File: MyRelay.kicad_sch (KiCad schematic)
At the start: 8 parts, among them K3 Relay, Q1 2N7002, Q2 2N7002

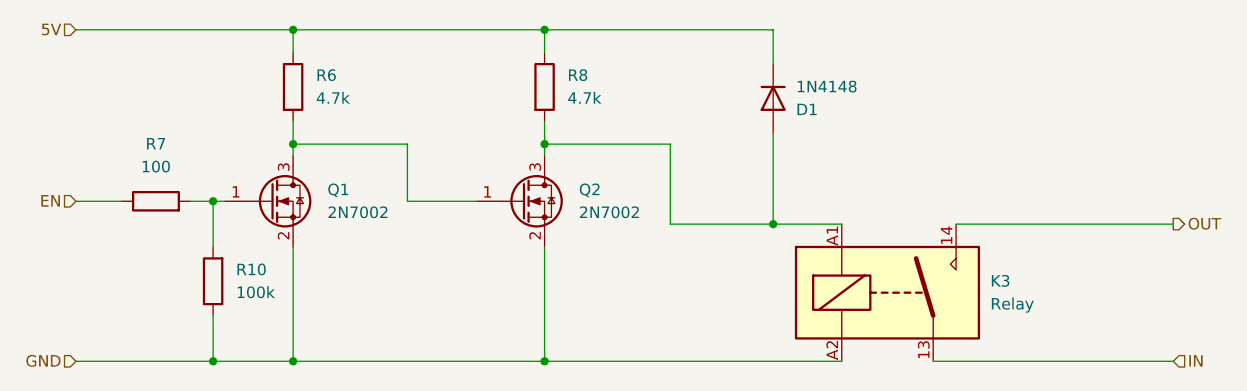
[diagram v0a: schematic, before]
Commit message: update footprints, add 230v module, use SSRs and do some basic layouting
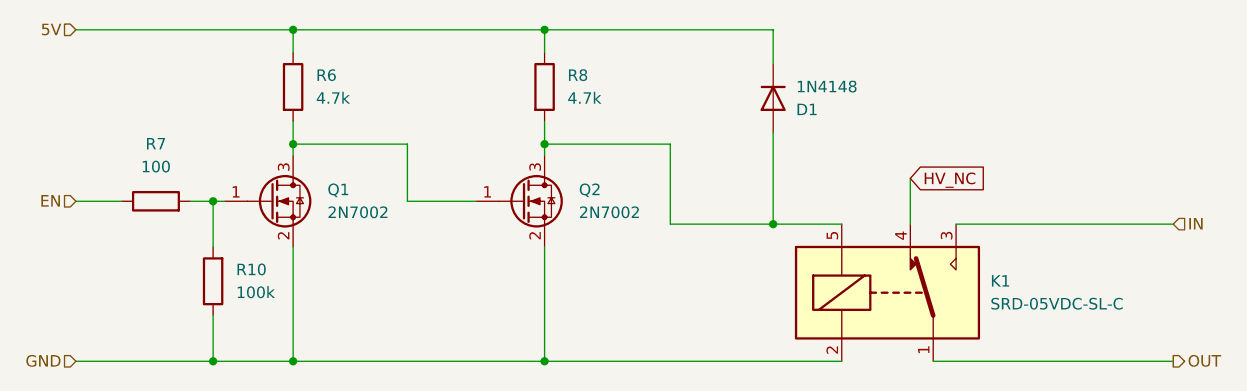
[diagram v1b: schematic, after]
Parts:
- removed K3: Relay, Relay_THT:Relay_SPST-NO_Fujitsu_FTR-LYAA005x_FormA_Vertical, symbol Relay:Fujitsu_FTR-LYAA005x
- added K1: SRD-05VDC-SL-C, Relay_THT:Relay_SPDT_SANYOU_SRD_Series_Form_C, symbol Relay:SANYOU_SRD_Form_C
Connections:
- net GND: now also K1.2
- net IN: now also K1.3
- net OUT: now also K1.1
- net at D1.2 (A), Q2.3 (D), R8.2: now also K1.5
- new net HV_NC: K1.4
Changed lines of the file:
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@@
+	(wire
+		(pts
+			(xy 138.43 97.79) (xy 162.56 97.79)
+		)
+		(stroke
+			(width 0)
+			(type default)
+		)
+	)
+	(wire
+		(pts
+			(xy 133.35 92.71) (xy 133.35 97.79)
+		)
+		(stroke
+			(width 0)
+			(type default)
+		)
+	)
 	(wire
 		(pts
@@
 	(wire
 		(pts
-			(xy 138.43 97.79) (xy 162.56 97.79)
-		)
-		(stroke
-			(width 0)
-			(type default)
-		)
-	)
-	(wire
-		(pts
 			(xy 64.77 86.36) (xy 64.77 88.9)
 		)
@@
 			(width 0)
 			(type default)
+		)
+	)
+	(global_label "HV_NC"
+		(shape input)
+		(at 133.35 92.71 0)
+		(fields_autoplaced yes)
+		(effects
+			(font
+				(size 1.27 1.27)
+			)
+			(justify left)
+		)
+		(property "Intersheetrefs" "${INTERSHEET_REFS}"
+			(at 142.3224 92.71 0)
+			(effects
+				(font
+					(size 1.27 1.27)
+				)
+				(justify left)
+				(hide yes)
+			)
 		)
 	)
@@
 		)
 	)
-	(hierarchical_label "OUT"
-		(shape output)
-		(at 162.56 97.79 0)
-		(effects
-			(font
-				(size 1.27 1.27)
-			)
-			(justify left)
-		)
-	)
 	(hierarchical_label "EN"
 		(shape input)
@@
 	(hierarchical_label "IN"
 		(shape input)
+		(at 162.56 97.79 0)
+		(effects
+			(font
+				(size 1.27 1.27)
+			)
+			(justify left)
+		)
+	)
+	(hierarchical_label "OUT"
+		(shape output)
 		(at 162.56 113.03 0)
 		(effects
@@
 	)
 	(symbol
+		(lib_id "Relay:SANYOU_SRD_Form_C")
+		(at 130.81 105.41 0)
+		(unit 1)
+		(exclude_from_sim no)
+		(in_bom yes)
+		(on_board yes)
+		(dnp no)
+		(fields_autoplaced yes)
+		(property "Reference" "K1"
+			(at 142.24 104.1399 0)
+			(effects
+				(font
+					(size 1.27 1.27)
+				)
+				(justify left)
+			)
+		)
+		(property "Value" "SRD-05VDC-SL-C"
+			(at 142.24 106.6799 0)
+			(effects
+				(font
+					(size 1.27 1.27)
+				)
+				(justify left)
+			)
+		)
+		(property "Footprint" "Relay_THT:Relay_SPDT_SANYOU_SRD_Series_Form_C"
+			(at 142.24 106.68 0)
+			(effects
+				(font
+					(size 1.27 1.27)
+				)
+				(justify left)
+				(hide yes)
+			)
+		)
+		(property "Datasheet" "http://www.sanyourelay.ca/public/products/pdf/SRD.pdf"
+			(at 130.81 105.41 0)
+			(effects
+				(font
+					(size 1.27 1.27)
+				)
+				(hide yes)
+			)
+		)
+		(property "Description" "Sanyo SRD relay, Single Pole Miniature Power Relay,"
+			(at 130.81 105.41 0)
+			(effects
+				(font
+					(size 1.27 1.27)
+				)
+				(hide yes)
+			)
+		)
+		(pin "4"
+		)
+		(pin "2"
+		)
+		(pin "5"
+		)
+		(pin "1"
+		)
+		(pin "3"
+		)
+		(instances
+			(project ""
+				(path "/18f69721-6a2b-4a2b-8e72-291680dbbe9a/9be4a7bd-c700-4299-b6e8-c4d6e64335b9"
+					(reference "K1")
+					(unit 1)
+				)
+				(path "/18f69721-6a2b-4a2b-8e72-291680dbbe9a/b03a6577-379d-4caf-acb6-2da9cef35c55"
+					(reference "K2")
+					(unit 1)
+				)
+			)
+		)
+	)
+	(symbol
 		(lib_id "Device:R")
 		(at 92.71 82.55 0)
@@
 					(unit 1)
 				)
-			)
-		)
-	)
-	(symbol
-		(lib_id "Relay:Fujitsu_FTR-LYAA005x")
-		(at 130.81 105.41 0)
-		(unit 1)
-		(exclude_from_sim no)
-		(in_bom yes)
-		(on_board yes)
-		(dnp no)
-		(fields_autoplaced yes)
-		(property "Reference" "K3"
-			(at 142.24 104.1399 0)
-			(effects
-				(font
-					(size 1.27 1.27)
-				)
-				(justify left)
-			)
-		)
-		(property "Value" "Relay"
-			(at 142.24 106.6799 0)
-			(effects
-				(font
-					(size 1.27 1.27)
-				)
-				(justify left)
-			)
-		)
-		(property "Footprint" "Relay_THT:Relay_SPST-NO_Fujitsu_FTR-LYAA005x_FormA_Vertical"
-			(at 142.24 106.68 0)
-			(effects
-				(font
-					(size 1.27 1.27)
-				)
-				(justify left)
-				(hide yes)
-			)
-		)
-		(property "Datasheet" "https://www.fujitsu.com/sg/imagesgig5/ftr-ly.pdf"
-			(at 148.59 109.22 0)
-			(effects
-				(font
-					(size 1.27 1.27)
-				)
-				(justify left)
-				(hide yes)
-			)
-		)
-		(property "Description" "Relay, SPST Form A, vertical mount, 5-60V coil, 6A, 250VAC, 28 x 5 x 15mm"
-			(at 130.81 105.41 0)
-			(effects
-				(font
-					(size 1.27 1.27)
-				)
-				(hide yes)
-			)
-		)
-		(property "LCSC" "C35449"
-			(at 142.24 104.1399 0)
-			(effects
-				(font
-					(size 1.27 1.27)
-				)
-				(hide yes)
-			)
-		)
-		(pin "14"
-		)
-		(pin "A2"
-		)
-		(pin "A1"
-		)
-		(pin "13"
-		)
-		(instances
-			(project ""
-				(path "/18f69721-6a2b-4a2b-8e72-291680dbbe9a/9be4a7bd-c700-4299-b6e8-c4d6e64335b9"
-					(reference "K3")
-					(unit 1)
-				)
-				(path "/18f69721-6a2b-4a2b-8e72-291680dbbe9a/b03a6577-379d-4caf-acb6-2da9cef35c55"
-					(reference "K4")
-					(unit 1)
-				)
